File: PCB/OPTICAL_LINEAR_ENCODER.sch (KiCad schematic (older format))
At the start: 6 parts, among them U10 ITR8307, U9 ITR8307

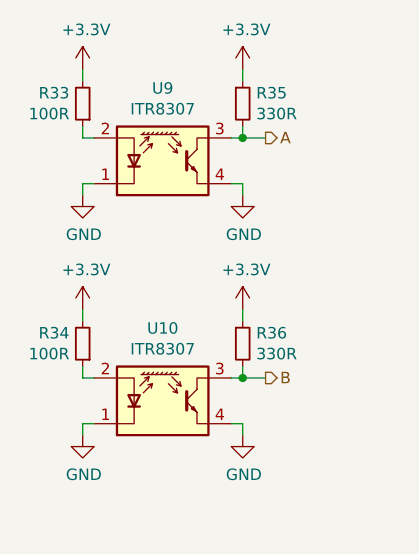
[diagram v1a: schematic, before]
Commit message: Increased VCC from 3v3 to 5v
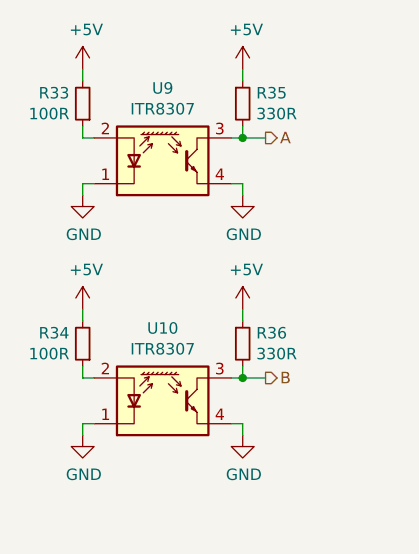
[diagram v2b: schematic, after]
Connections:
- net +3V3 renamed +5V
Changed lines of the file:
@@
 $Descr A4 11693 8268
 encoding utf-8
-Sheet 21 25
+Sheet 22 25
 Title ""
 Date ""
@@
 $EndComp
 $Comp
-L power:+3.3V #PWR0143
-U 1 1 5E905CF2
-P 5500 3000
-F 0 "#PWR0143" H 5500 2850 50  0001 C CNN
-F 1 "+3.3V" H 5515 3173 50  0000 C CNN
-F 2 "" H 5500 3000 50  0001 C CNN
-F 3 "" H 5500 3000 50  0001 C CNN
-	1    5500 3000
-	1    0    0    -1
-$EndComp
-$Comp
-L power:+3.3V #PWR0147
-U 1 1 5E905EA1
-P 6200 3000
-F 0 "#PWR0147" H 6200 2850 50  0001 C CNN
-F 1 "+3.3V" H 6215 3173 50  0000 C CNN
-F 2 "" H 6200 3000 50  0001 C CNN
-F 3 "" H 6200 3000 50  0001 C CNN
-	1    6200 3000
-	1    0    0    -1
-$EndComp
-$Comp
 L power:GND #PWR0144
 U 1 1 5E908152
@@
 $EndComp
 $Comp
-L power:+3.3V #PWR0145
-U 1 1 5E90CA53
-P 5500 4050
-F 0 "#PWR0145" H 5500 3900 50  0001 C CNN
-F 1 "+3.3V" H 5515 4223 50  0000 C CNN
-F 2 "" H 5500 4050 50  0001 C CNN
-F 3 "" H 5500 4050 50  0001 C CNN
-	1    5500 4050
-	1    0    0    -1
-$EndComp
-$Comp
-L power:+3.3V #PWR0149
-U 1 1 5E90CA59
-P 6200 4050
-F 0 "#PWR0149" H 6200 3900 50  0001 C CNN
-F 1 "+3.3V" H 6215 4223 50  0000 C CNN
-F 2 "" H 6200 4050 50  0001 C CNN
-F 3 "" H 6200 4050 50  0001 C CNN
-	1    6200 4050
-	1    0    0    -1
-$EndComp
-$Comp
 L power:GND #PWR0146
 U 1 1 5E90CA5F
@@
 	6300 4350 6200 4350
 Connection ~ 6200 4350
+$Comp
+L power:+5V #PWR?
+U 1 1 5E90C9D7
+P 5500 3000
+AR Path="/5E8A6686/5E90C9D7" Ref="#PWR?"  Part="1"
+AR Path="/5E90196F/5E90C9D7" Ref="#PWR?"  Part="1"
+F 0 "#PWR?" H 5500 2850 50  0001 C CNN
+F 1 "+5V" H 5515 3173 50  0000 C CNN
+F 2 "" H 5500 3000 50  0001 C CNN
+F 3 "" H 5500 3000 50  0001 C CNN
+	1    5500 3000
+	1    0    0    -1
+$EndComp
+$Comp
+L power:+5V #PWR?
+U 1 1 5E90CC67
+P 6200 3000
+AR Path="/5E8A6686/5E90CC67" Ref="#PWR?"  Part="1"
+AR Path="/5E90196F/5E90CC67" Ref="#PWR?"  Part="1"
+F 0 "#PWR?" H 6200 2850 50  0001 C CNN
+F 1 "+5V" H 6215 3173 50  0000 C CNN
+F 2 "" H 6200 3000 50  0001 C CNN
+F 3 "" H 6200 3000 50  0001 C CNN
+	1    6200 3000
+	1    0    0    -1
+$EndComp
+$Comp
+L power:+5V #PWR?
+U 1 1 5E90CF93
+P 5500 4050
+AR Path="/5E8A6686/5E90CF93" Ref="#PWR?"  Part="1"
+AR Path="/5E90196F/5E90CF93" Ref="#PWR?"  Part="1"
+F 0 "#PWR?" H 5500 3900 50  0001 C CNN
+F 1 "+5V" H 5515 4223 50  0000 C CNN
+F 2 "" H 5500 4050 50  0001 C CNN
+F 3 "" H 5500 4050 50  0001 C CNN
+	1    5500 4050
+	1    0    0    -1
+$EndComp
+$Comp
+L power:+5V #PWR?
+U 1 1 5E90D293
+P 6200 4050
+AR Path="/5E8A6686/5E90D293" Ref="#PWR?"  Part="1"
+AR Path="/5E90196F/5E90D293" Ref="#PWR?"  Part="1"
+F 0 "#PWR?" H 6200 3900 50  0001 C CNN
+F 1 "+5V" H 6215 4223 50  0000 C CNN
+F 2 "" H 6200 4050 50  0001 C CNN
+F 3 "" H 6200 4050 50  0001 C CNN
+	1    6200 4050
+	1    0    0    -1
+$EndComp
 $EndSCHEMATC

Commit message: Added Humidity and temperature sensors
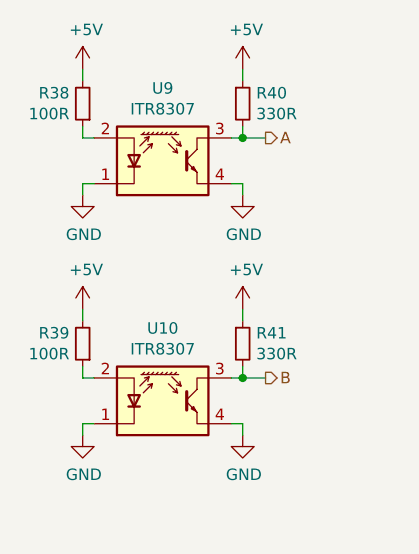
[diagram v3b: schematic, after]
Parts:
- renumbered R33 to R38, R34 to R39, R35 to R40, R36 to R41
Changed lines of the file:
@@
 $EndComp
 $Comp
-L Device:R_Small R35
+L Device:R_Small R40
 U 1 1 5E90496B
 P 6200 3150
-F 0 "R35" H 6259 3196 50  0000 L CNN
+F 0 "R40" H 6259 3196 50  0000 L CNN
 F 1 "330R" H 6259 3105 50  0000 L CNN
 F 2 "" H 6200 3150 50  0001 C CNN
@@
 $EndComp
 $Comp
-L Device:R_Small R33
+L Device:R_Small R38
 U 1 1 5E905250
 P 5500 3150
-F 0 "R33" H 5558 3104 50  0000 L CNN
+F 0 "R38" H 5558 3104 50  0000 L CNN
 F 1 "100R" H 5558 3195 50  0000 L CNN
 F 2 "" H 5500 3150 50  0001 C CNN
@@
 $EndComp
 $Comp
-L power:GND #PWR0144
+L power:GND #PWR0147
 U 1 1 5E908152
 P 5500 3550
-F 0 "#PWR0144" H 5500 3300 50  0001 C CNN
+F 0 "#PWR0147" H 5500 3300 50  0001 C CNN
 F 1 "GND" H 5505 3377 50  0000 C CNN
 F 2 "" H 5500 3550 50  0001 C CNN
@@
 $EndComp
 $Comp
-L power:GND #PWR0148
+L power:GND #PWR0151
 U 1 1 5E90833E
 P 6200 3550
-F 0 "#PWR0148" H 6200 3300 50  0001 C CNN
+F 0 "#PWR0151" H 6200 3300 50  0001 C CNN
 F 1 "GND" H 6205 3377 50  0000 C CNN
 F 2 "" H 6200 3550 50  0001 C CNN
@@
 $EndComp
 $Comp
-L Device:R_Small R36
+L Device:R_Small R41
 U 1 1 5E90CA47
 P 6200 4200
-F 0 "R36" H 6259 4246 50  0000 L CNN
+F 0 "R41" H 6259 4246 50  0000 L CNN
 F 1 "330R" H 6259 4155 50  0000 L CNN
 F 2 "" H 6200 4200 50  0001 C CNN
@@
 $EndComp
 $Comp
-L Device:R_Small R34
+L Device:R_Small R39
 U 1 1 5E90CA4D
 P 5500 4200
-F 0 "R34" H 5558 4154 50  0000 L CNN
+F 0 "R39" H 5558 4154 50  0000 L CNN
 F 1 "100R" H 5558 4245 50  0000 L CNN
 F 2 "" H 5500 4200 50  0001 C CNN
@@
 $EndComp
 $Comp
-L power:GND #PWR0146
+L power:GND #PWR0149
 U 1 1 5E90CA5F
 P 5500 4600
-F 0 "#PWR0146" H 5500 4350 50  0001 C CNN
+F 0 "#PWR0149" H 5500 4350 50  0001 C CNN
 F 1 "GND" H 5505 4427 50  0000 C CNN
 F 2 "" H 5500 4600 50  0001 C CNN
@@
 $EndComp
 $Comp
-L power:GND #PWR0150
+L power:GND #PWR0153
 U 1 1 5E90CA65
 P 6200 4600
-F 0 "#PWR0150" H 6200 4350 50  0001 C CNN
+F 0 "#PWR0153" H 6200 4350 50  0001 C CNN
 F 1 "GND" H 6205 4427 50  0000 C CNN
 F 2 "" H 6200 4600 50  0001 C CNN
@@
 P 5500 3000
 AR Path="/5E8A6686/5E90C9D7" Ref="#PWR?"  Part="1"
-AR Path="/5E90196F/5E90C9D7" Ref="#PWR?"  Part="1"
-F 0 "#PWR?" H 5500 2850 50  0001 C CNN
+AR Path="/5E90196F/5E90C9D7" Ref="#PWR0146"  Part="1"
+F 0 "#PWR0146" H 5500 2850 50  0001 C CNN
 F 1 "+5V" H 5515 3173 50  0000 C CNN
 F 2 "" H 5500 3000 50  0001 C CNN
@@
 P 6200 3000
 AR Path="/5E8A6686/5E90CC67" Ref="#PWR?"  Part="1"
-AR Path="/5E90196F/5E90CC67" Ref="#PWR?"  Part="1"
-F 0 "#PWR?" H 6200 2850 50  0001 C CNN
+AR Path="/5E90196F/5E90CC67" Ref="#PWR0150"  Part="1"
+F 0 "#PWR0150" H 6200 2850 50  0001 C CNN
 F 1 "+5V" H 6215 3173 50  0000 C CNN
 F 2 "" H 6200 3000 50  0001 C CNN
@@
 P 5500 4050
 AR Path="/5E8A6686/5E90CF93" Ref="#PWR?"  Part="1"
-AR Path="/5E90196F/5E90CF93" Ref="#PWR?"  Part="1"
-F 0 "#PWR?" H 5500 3900 50  0001 C CNN
+AR Path="/5E90196F/5E90CF93" Ref="#PWR0148"  Part="1"
+F 0 "#PWR0148" H 5500 3900 50  0001 C CNN
 F 1 "+5V" H 5515 4223 50  0000 C CNN
 F 2 "" H 5500 4050 50  0001 C CNN
@@
 P 6200 4050
 AR Path="/5E8A6686/5E90D293" Ref="#PWR?"  Part="1"
-AR Path="/5E90196F/5E90D293" Ref="#PWR?"  Part="1"
-F 0 "#PWR?" H 6200 3900 50  0001 C CNN
+AR Path="/5E90196F/5E90D293" Ref="#PWR0152"  Part="1"
+F 0 "#PWR0152" H 6200 3900 50  0001 C CNN
 F 1 "+5V" H 6215 4223 50  0000 C CNN
 F 2 "" H 6200 4050 50  0001 C CNN

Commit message: Added remaining test points
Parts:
- added TP38: A, symbol Connector:TestPoint
- added TP39: B, symbol Connector:TestPoint
- renumbered R38 to R35, R39 to R36, R40 to R37, R41 to R38, U9 to U13, U10 to U14
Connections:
- wire segments 22 -> 26
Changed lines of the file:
@@
 $EndDescr
 $Comp
-L Sensor_Proximity:ITR8307 U9
+L Sensor_Proximity:ITR8307 U13
 U 1 1 5E901D68
 P 5850 3400
-F 0 "U9" H 5850 3717 50  0000 C CNN
+F 0 "U13" H 5850 3717 50  0000 C CNN
 F 1 "ITR8307" H 5850 3626 50  0000 C CNN
 F 2 "custom:ITR8307-L24-TR8" H 5850 3200 50  0001 C CNN
@@
 $EndComp
 $Comp
-L Device:R_Small R40
+L Device:R_Small R37
 U 1 1 5E90496B
 P 6200 3150
-F 0 "R40" H 6259 3196 50  0000 L CNN
+F 0 "R37" H 6259 3196 50  0000 L CNN
 F 1 "330R" H 6259 3105 50  0000 L CNN
 F 2 "" H 6200 3150 50  0001 C CNN
@@
 $EndComp
 $Comp
-L Device:R_Small R38
+L Device:R_Small R35
 U 1 1 5E905250
 P 5500 3150
-F 0 "R38" H 5558 3104 50  0000 L CNN
+F 0 "R35" H 5558 3104 50  0000 L CNN
 F 1 "100R" H 5558 3195 50  0000 L CNN
 F 2 "" H 5500 3150 50  0001 C CNN
@@
 $EndComp
 $Comp
-L power:GND #PWR0147
+L power:GND #PWR0136
 U 1 1 5E908152
 P 5500 3550
-F 0 "#PWR0147" H 5500 3300 50  0001 C CNN
+F 0 "#PWR0136" H 5500 3300 50  0001 C CNN
 F 1 "GND" H 5505 3377 50  0000 C CNN
 F 2 "" H 5500 3550 50  0001 C CNN
@@
 $EndComp
 $Comp
-L power:GND #PWR0151
+L power:GND #PWR0140
 U 1 1 5E90833E
 P 6200 3550
-F 0 "#PWR0151" H 6200 3300 50  0001 C CNN
+F 0 "#PWR0140" H 6200 3300 50  0001 C CNN
 F 1 "GND" H 6205 3377 50  0000 C CNN
 F 2 "" H 6200 3550 50  0001 C CNN
@@
 Wire Wire Line
 	6200 3500 6200 3550
-Text HLabel 6300 3300 2    50   Output ~ 0
+Text HLabel 6400 3300 2    50   Output ~ 0
 A
 Wire Wire Line
-	6300 3300 6200 3300
+	6400 3300 6300 3300
 Connection ~ 6200 3300
 $Comp
-L Sensor_Proximity:ITR8307 U10
+L Sensor_Proximity:ITR8307 U14
 U 1 1 5E90CA41
 P 5850 4450
-F 0 "U10" H 5850 4767 50  0000 C CNN
+F 0 "U14" H 5850 4767 50  0000 C CNN
 F 1 "ITR8307" H 5850 4676 50  0000 C CNN
 F 2 "custom:ITR8307-L24-TR8" H 5850 4250 50  0001 C CNN
@@
 $EndComp
 $Comp
-L Device:R_Small R41
+L Device:R_Small R38
 U 1 1 5E90CA47
 P 6200 4200
-F 0 "R41" H 6259 4246 50  0000 L CNN
+F 0 "R38" H 6259 4246 50  0000 L CNN
 F 1 "330R" H 6259 4155 50  0000 L CNN
 F 2 "" H 6200 4200 50  0001 C CNN
@@
 $EndComp
 $Comp
-L Device:R_Small R39
+L Device:R_Small R36
 U 1 1 5E90CA4D
 P 5500 4200
-F 0 "R39" H 5558 4154 50  0000 L CNN
+F 0 "R36" H 5558 4154 50  0000 L CNN
 F 1 "100R" H 5558 4245 50  0000 L CNN
 F 2 "" H 5500 4200 50  0001 C CNN
@@
 $EndComp
 $Comp
-L power:GND #PWR0149
+L power:GND #PWR0138
 U 1 1 5E90CA5F
 P 5500 4600
-F 0 "#PWR0149" H 5500 4350 50  0001 C CNN
+F 0 "#PWR0138" H 5500 4350 50  0001 C CNN
 F 1 "GND" H 5505 4427 50  0000 C CNN
 F 2 "" H 5500 4600 50  0001 C CNN
@@
 $EndComp
 $Comp
-L power:GND #PWR0153
+L power:GND #PWR0142
 U 1 1 5E90CA65
 P 6200 4600
-F 0 "#PWR0153" H 6200 4350 50  0001 C CNN
+F 0 "#PWR0142" H 6200 4350 50  0001 C CNN
 F 1 "GND" H 6205 4427 50  0000 C CNN
 F 2 "" H 6200 4600 50  0001 C CNN
@@
 Wire Wire Line
 	6200 4550 6200 4600
-Text HLabel 6300 4350 2    50   Output ~ 0
+Text HLabel 6400 4350 2    50   Output ~ 0
 B
 Wire Wire Line
-	6300 4350 6200 4350
+	6400 4350 6300 4350
 Connection ~ 6200 4350
 $Comp
@@
 P 5500 3000
 AR Path="/5E8A6686/5E90C9D7" Ref="#PWR?"  Part="1"
-AR Path="/5E90196F/5E90C9D7" Ref="#PWR0146"  Part="1"
-F 0 "#PWR0146" H 5500 2850 50  0001 C CNN
+AR Path="/5E90196F/5E90C9D7" Ref="#PWR0135"  Part="1"
+F 0 "#PWR0135" H 5500 2850 50  0001 C CNN
 F 1 "+5V" H 5515 3173 50  0000 C CNN
 F 2 "" H 5500 3000 50  0001 C CNN
@@
 P 6200 3000
 AR Path="/5E8A6686/5E90CC67" Ref="#PWR?"  Part="1"
-AR Path="/5E90196F/5E90CC67" Ref="#PWR0150"  Part="1"
-F 0 "#PWR0150" H 6200 2850 50  0001 C CNN
+AR Path="/5E90196F/5E90CC67" Ref="#PWR0139"  Part="1"
+F 0 "#PWR0139" H 6200 2850 50  0001 C CNN
 F 1 "+5V" H 6215 3173 50  0000 C CNN
 F 2 "" H 6200 3000 50  0001 C CNN
@@
 P 5500 4050
 AR Path="/5E8A6686/5E90CF93" Ref="#PWR?"  Part="1"
-AR Path="/5E90196F/5E90CF93" Ref="#PWR0148"  Part="1"
-F 0 "#PWR0148" H 5500 3900 50  0001 C CNN
+AR Path="/5E90196F/5E90CF93" Ref="#PWR0137"  Part="1"
+F 0 "#PWR0137" H 5500 3900 50  0001 C CNN
 F 1 "+5V" H 5515 4223 50  0000 C CNN
 F 2 "" H 5500 4050 50  0001 C CNN
@@
 P 6200 4050
 AR Path="/5E8A6686/5E90D293" Ref="#PWR?"  Part="1"
-AR Path="/5E90196F/5E90D293" Ref="#PWR0152"  Part="1"
-F 0 "#PWR0152" H 6200 3900 50  0001 C CNN
+AR Path="/5E90196F/5E90D293" Ref="#PWR0141"  Part="1"
+F 0 "#PWR0141" H 6200 3900 50  0001 C CNN
 F 1 "+5V" H 6215 4223 50  0000 C CNN
 F 2 "" H 6200 4050 50  0001 C CNN
@@
 	1    0    0    -1
 $EndComp
+$Comp
+L Connector:TestPoint TP?
+U 1 1 5E9D1DF6
+P 6300 4450
+AR Path="/5E9D1DF6" Ref="TP?"  Part="1"
+AR Path="/5E90196F/5E9D1DF6" Ref="TP39"  Part="1"
+F 0 "TP39" H 6242 4476 50  0000 R CNN
+F 1 "B" H 6242 4567 50  0000 R CNN
+F 2 "" H 6500 4450 50  0001 C CNN
+F 3 "~" H 6500 4450 50  0001 C CNN
+	1    6300 4450
+	-1   0    0    1
+$EndComp
+Wire Wire Line
+	6300 4450 6300 4350
+Connection ~ 6300 4350
+Wire Wire Line
+	6300 4350 6200 4350
+$Comp
+L Connector:TestPoint TP?
+U 1 1 5E9D3A24
+P 6300 3400
+AR Path="/5E9D3A24" Ref="TP?"  Part="1"
+AR Path="/5E90196F/5E9D3A24" Ref="TP38"  Part="1"
+F 0 "TP38" H 6242 3426 50  0000 R CNN
+F 1 "A" H 6242 3517 50  0000 R CNN
+F 2 "" H 6500 3400 50  0001 C CNN
+F 3 "~" H 6500 3400 50  0001 C CNN
+	1    6300 3400
+	-1   0    0    1
+$EndComp
+Wire Wire Line
+	6300 3400 6300 3300
+Connection ~ 6300 3300
+Wire Wire Line
+	6300 3300 6200 3300
 $EndSCHEMATC

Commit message: Added majority footprints
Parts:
- R35, R36, R37, R38: footprint (none) -> Resistor_SMD:R_0603_1608Metric
- TP38, TP39: footprint (none) -> custom:TestPoint_Pad_D1.5mm
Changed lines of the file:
@@
 F 0 "R37" H 6259 3196 50  0000 L CNN
 F 1 "330R" H 6259 3105 50  0000 L CNN
-F 2 "" H 6200 3150 50  0001 C CNN
+F 2 "Resistor_SMD:R_0603_1608Metric" H 6200 3150 50  0001 C CNN
 F 3 "~" H 6200 3150 50  0001 C CNN
 	1    6200 3150
@@
 F 0 "R35" H 5558 3104 50  0000 L CNN
 F 1 "100R" H 5558 3195 50  0000 L CNN
-F 2 "" H 5500 3150 50  0001 C CNN
+F 2 "Resistor_SMD:R_0603_1608Metric" H 5500 3150 50  0001 C CNN
 F 3 "~" H 5500 3150 50  0001 C CNN
 	1    5500 3150
@@
 F 0 "R38" H 6259 4246 50  0000 L CNN
 F 1 "330R" H 6259 4155 50  0000 L CNN
-F 2 "" H 6200 4200 50  0001 C CNN
+F 2 "Resistor_SMD:R_0603_1608Metric" H 6200 4200 50  0001 C CNN
 F 3 "~" H 6200 4200 50  0001 C CNN
 	1    6200 4200
@@
 F 0 "R36" H 5558 4154 50  0000 L CNN
 F 1 "100R" H 5558 4245 50  0000 L CNN
-F 2 "" H 5500 4200 50  0001 C CNN
+F 2 "Resistor_SMD:R_0603_1608Metric" H 5500 4200 50  0001 C CNN
 F 3 "~" H 5500 4200 50  0001 C CNN
 	1    5500 4200
@@
 F 0 "TP39" H 6242 4476 50  0000 R CNN
 F 1 "B" H 6242 4567 50  0000 R CNN
-F 2 "" H 6500 4450 50  0001 C CNN
+F 2 "custom:TestPoint_Pad_D1.5mm" H 6500 4450 50  0001 C CNN
 F 3 "~" H 6500 4450 50  0001 C CNN
 	1    6300 4450
@@
 F 0 "TP38" H 6242 3426 50  0000 R CNN
 F 1 "A" H 6242 3517 50  0000 R CNN
-F 2 "" H 6500 3400 50  0001 C CNN
+F 2 "custom:TestPoint_Pad_D1.5mm" H 6500 3400 50  0001 C CNN
 F 3 "~" H 6500 3400 50  0001 C CNN
 	1    6300 3400
